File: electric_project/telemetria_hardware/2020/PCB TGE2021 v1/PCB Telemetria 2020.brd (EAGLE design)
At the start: 160 x 100 mm, 16 parts, among them IC1 INA240A1DR, IC2 MCP3221A6T-E_OTVAO, IC3 AZ1117IH-3.3TRG1

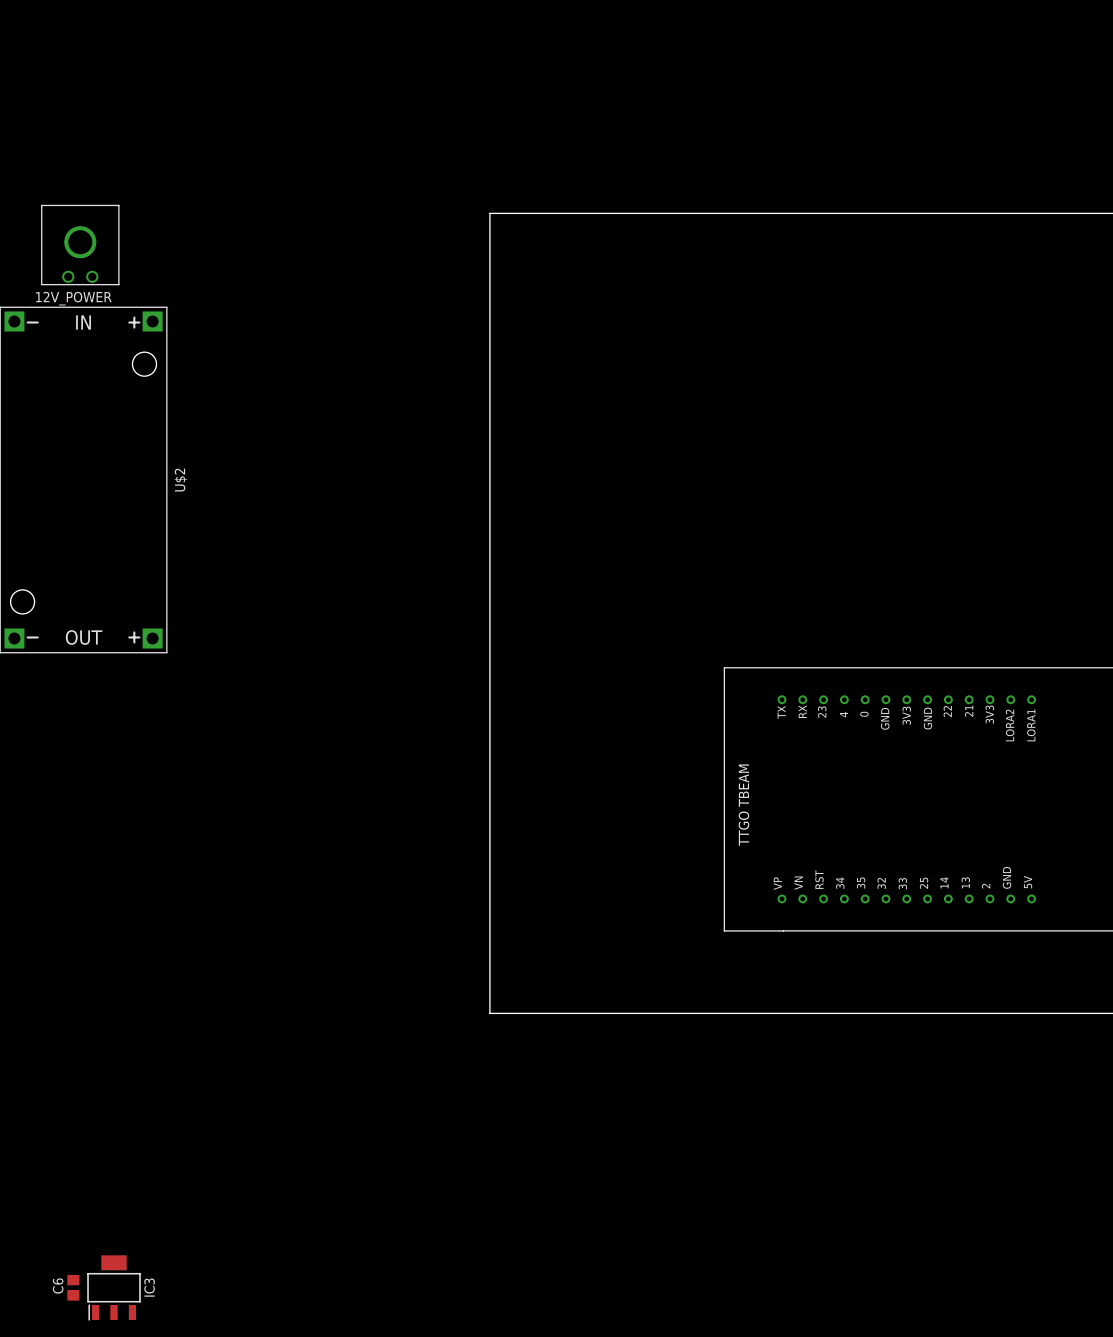
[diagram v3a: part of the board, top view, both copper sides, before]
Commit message: Ajustes de posicionamento no sch e brd
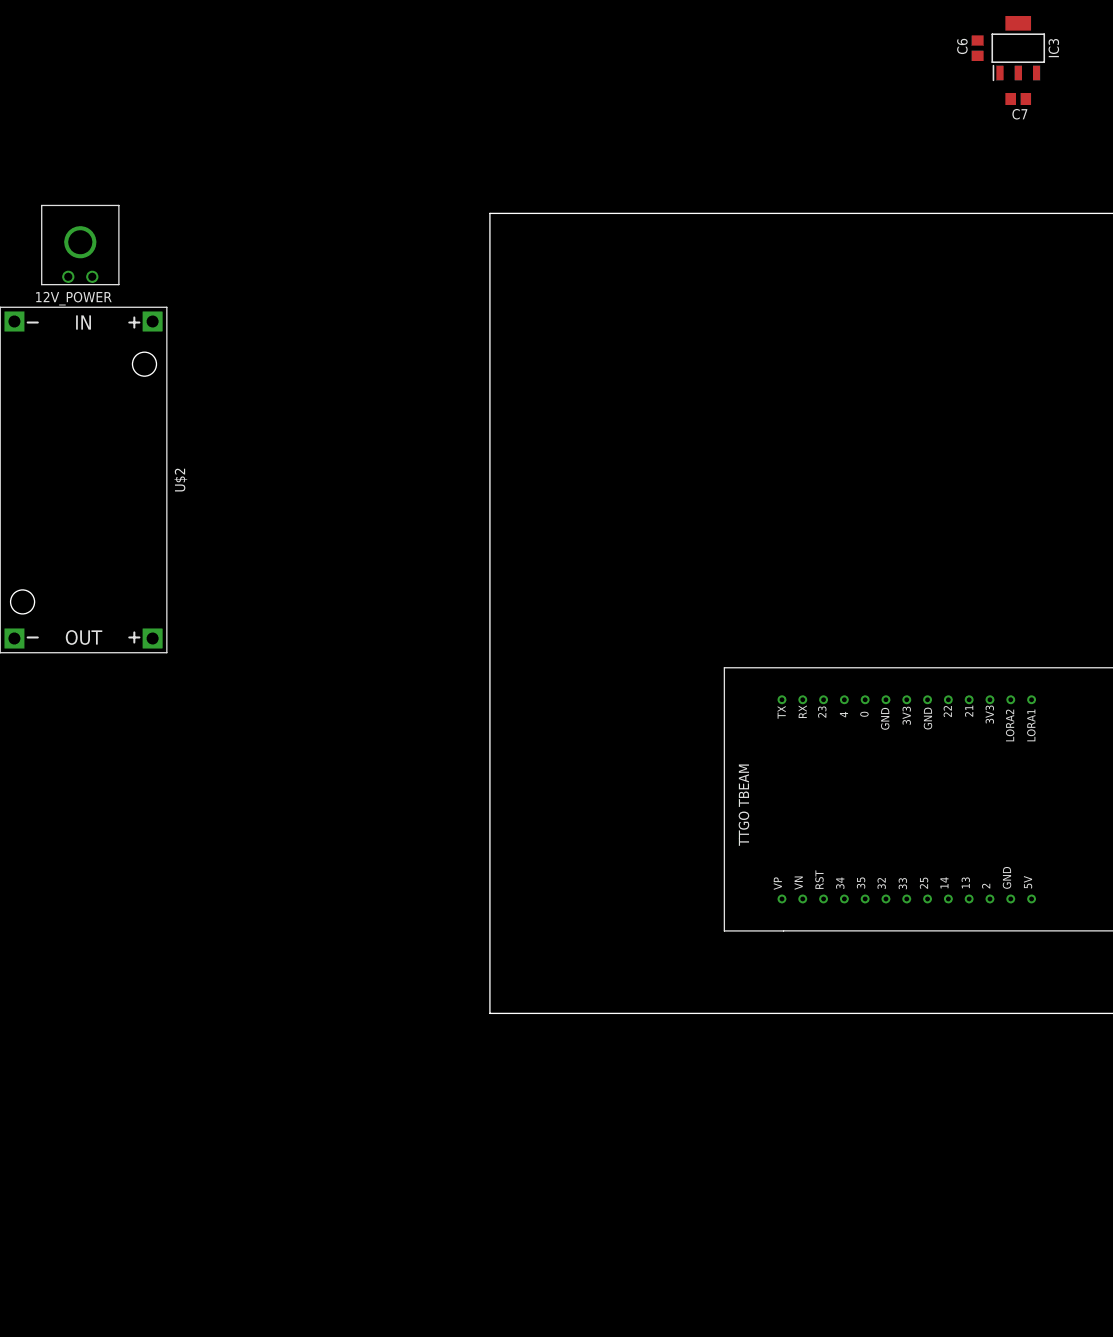
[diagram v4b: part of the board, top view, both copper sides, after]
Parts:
- added C7: 22uF, rcl:C0805
- moved C6 191.8 mm to (61.0, 120.7)
- moved IC3 191.8 mm to (66.0, 120.7)
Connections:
- net GND: now also C7.2
- net VCC_5V: now also C7.1
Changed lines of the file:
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@@
 <attribute name="VALUE" x="-52.705" y="92.075" size="1.27" layer="27" rot="R180" align="center"/>
 </element>
-<element name="IC3" library="AZ1117IH-3.3TRG1" package="SOT230P700X170-4N" value="AZ1117IH-3.3TRG1" x="-46.99" y="-34.29" smashed="yes" rot="R90">
-<attribute name="DESCRIPTION" value="LDO Voltage Regulators LDO BJT HiCurr 1.35A 10Hz to 10KHz" x="-46.99" y="-34.29" size="1.778" layer="27" rot="R90" display="off"/>
-<attribute name="HEIGHT" value="1.7mm" x="-46.99" y="-34.29" size="1.778" layer="27" rot="R90" display="off"/>
-<attribute name="MANUFACTURER_NAME" value="Diodes Inc." x="-46.99" y="-34.29" size="1.778" layer="27" rot="R90" display="off"/>
-<attribute name="MANUFACTURER_PART_NUMBER" value="AZ1117IH-3.3TRG1" x="-46.99" y="-34.29" size="1.778" layer="27" rot="R90" display="off"/>
-<attribute name="MOUSER_PART_NUMBER" value="621-AZ1117IH-3.3TRG1" x="-46.99" y="-34.29" size="1.778" layer="27" rot="R90" display="off"/>
-<attribute name="MOUSER_PRICE-STOCK" value="https://www.mouser.co.uk/ProductDetail/Diodes-Incorporated/AZ1117IH-33TRG1?qs=cpo3%2FpBou2jnS4SxLgAVoA%3D%3D" x="-46.99" y="-34.29" size="1.778" layer="27" rot="R90" display="off"/>
-<attribute name="NAME" x="-42.545" y="-34.29" size="1.27" layer="25" rot="R90" align="center"/>
-<attribute name="VALUE" x="-46.99" y="-34.29" size="1.27" layer="27" rot="R90" align="center"/>
+<element name="IC3" library="AZ1117IH-3.3TRG1" package="SOT230P700X170-4N" value="AZ1117IH-3.3TRG1" x="66.04" y="120.65" smashed="yes" rot="R90">
+<attribute name="DESCRIPTION" value="LDO Voltage Regulators LDO BJT HiCurr 1.35A 10Hz to 10KHz" x="66.04" y="120.65" size="1.778" layer="27" rot="R90" display="off"/>
+<attribute name="HEIGHT" value="1.7mm" x="66.04" y="120.65" size="1.778" layer="27" rot="R90" display="off"/>
+<attribute name="MANUFACTURER_NAME" value="Diodes Inc." x="66.04" y="120.65" size="1.778" layer="27" rot="R90" display="off"/>
+<attribute name="MANUFACTURER_PART_NUMBER" value="AZ1117IH-3.3TRG1" x="66.04" y="120.65" size="1.778" layer="27" rot="R90" display="off"/>
+<attribute name="MOUSER_PART_NUMBER" value="621-AZ1117IH-3.3TRG1" x="66.04" y="120.65" size="1.778" layer="27" rot="R90" display="off"/>
+<attribute name="MOUSER_PRICE-STOCK" value="https://www.mouser.co.uk/ProductDetail/Diodes-Incorporated/AZ1117IH-33TRG1?qs=cpo3%2FpBou2jnS4SxLgAVoA%3D%3D" x="66.04" y="120.65" size="1.778" layer="27" rot="R90" display="off"/>
+<attribute name="NAME" x="70.485" y="120.65" size="1.27" layer="25" rot="R90" align="center"/>
+<attribute name="VALUE" x="66.04" y="120.65" size="1.27" layer="27" rot="R90" align="center"/>
 </element>
-<element name="C6" library="rcl" library_urn="urn:adsk.eagle:library:334" package="C0805" package3d_urn="urn:adsk.eagle:package:23617/2" value="22uF" x="-52.07" y="-34.29" smashed="yes" rot="R270">
-<attribute name="NAME" x="-54.61" y="-33.02" size="1.27" layer="25" rot="R270"/>
-<attribute name="POPULARITY" value="63" x="-52.07" y="-34.29" size="1.778" layer="27" rot="R270" display="off"/>
-<attribute name="SPICEPREFIX" value="C" x="-52.07" y="-34.29" size="1.778" layer="27" rot="R270" display="off"/>
-<attribute name="VALUE" x="-54.61" y="-33.02" size="1.27" layer="27" rot="R270"/>
+<element name="C6" library="rcl" library_urn="urn:adsk.eagle:library:334" package="C0805" package3d_urn="urn:adsk.eagle:package:23617/2" value="22uF" x="60.96" y="120.65" smashed="yes" rot="R270">
+<attribute name="NAME" x="58.42" y="121.92" size="1.27" layer="25" rot="R270"/>
+<attribute name="POPULARITY" value="63" x="60.96" y="120.65" size="1.778" layer="27" rot="R270" display="off"/>
+<attribute name="SPICEPREFIX" value="C" x="60.96" y="120.65" size="1.778" layer="27" rot="R270" display="off"/>
+<attribute name="VALUE" x="58.42" y="121.92" size="1.27" layer="27" rot="R270"/>
+</element>
+<element name="C7" library="rcl" library_urn="urn:adsk.eagle:library:334" package="C0805" package3d_urn="urn:adsk.eagle:package:23617/2" value="22uF" x="66.04" y="114.3" smashed="yes" rot="R180">
+<attribute name="NAME" x="67.31" y="113.03" size="1.27" layer="25" rot="R180"/>
+<attribute name="POPULARITY" value="63" x="66.04" y="114.3" size="1.778" layer="27" rot="R180" display="off"/>
+<attribute name="SPICEPREFIX" value="C" x="66.04" y="114.3" size="1.778" layer="27" rot="R180" display="off"/>
+<attribute name="VALUE" x="67.31" y="116.84" size="1.27" layer="27" rot="R180"/>
 </element>
 </elements>
@@
 <contactref element="IC3" pad="1"/>
 <contactref element="C6" pad="2"/>
-<wire x1="65.105" y1="14.305" x2="49.505" y2="39.205" width="0" layer="19" extent="1-1"/>
-<wire x1="-59.436" y1="46.863" x2="49.505" y2="39.205" width="0" layer="19" extent="1-1"/>
+<contactref element="C7" pad="2"/>
+<wire x1="60.96" y1="119.7" x2="65.09" y2="114.3" width="0" layer="19" extent="1-1"/>
+<wire x1="63.74" y1="117.55" x2="60.96" y2="119.7" width="0" layer="19" extent="1-1"/>
+<wire x1="-59.436" y1="46.863" x2="60.96" y2="119.7" width="0" layer="19" extent="1-1"/>
 <wire x1="-59.436" y1="86.487" x2="-59.436" y2="46.863" width="0" layer="19" extent="1-1"/>
 <wire x1="-52.705" y1="92.075" x2="-59.436" y2="86.487" width="0" layer="19" extent="1-1"/>
-<wire x1="-49.29" y1="-37.39" x2="-59.436" y2="46.863" width="0" layer="19" extent="1-1"/>
-<wire x1="-52.07" y1="-35.24" x2="-49.29" y2="-37.39" width="0" layer="19" extent="1-1"/>
+<wire x1="49.505" y1="39.205" x2="-59.436" y2="46.863" width="0" layer="19" extent="1-1"/>
+<wire x1="65.105" y1="14.305" x2="49.505" y2="39.205" width="0" layer="19" extent="1-1"/>
 <wire x1="182.709" y1="97.155" x2="65.105" y2="14.305" width="0" layer="19" extent="1-1"/>
 <wire x1="188.131" y1="97.155" x2="182.709" y2="97.155" width="0" layer="19" extent="1-1"/>
@@
 <contactref element="IC3" pad="2"/>
 <wire x1="52.105" y1="39.205" x2="62.505" y2="39.205" width="0" layer="19" extent="1-1"/>
-<wire x1="-46.99" y1="-31.19" x2="52.105" y2="39.205" width="0" layer="19" extent="1-1"/>
-<wire x1="-46.99" y1="-37.39" x2="-46.99" y2="-31.19" width="0" layer="19" extent="1-1"/>
-<wire x1="-52.07" y1="-33.34" x2="-46.99" y2="-37.39" width="0" layer="19" extent="1-1"/>
+<wire x1="66.04" y1="123.75" x2="52.105" y2="39.205" width="0" layer="19" extent="1-1"/>
+<wire x1="66.04" y1="117.55" x2="66.04" y2="123.75" width="0" layer="19" extent="1-1"/>
+<wire x1="60.96" y1="121.6" x2="66.04" y2="117.55" width="0" layer="19" extent="1-1"/>
 <wire x1="180.34" y1="87.315" x2="62.505" y2="39.205" width="0" layer="19" extent="1-1"/>
 <wire x1="182.88" y1="87.315" x2="180.34" y2="87.315" width="0" layer="19" extent="1-1"/>
@@
 <contactref element="U$2" pad="OUT+"/>
 <contactref element="IC3" pad="3"/>
-<wire x1="-42.164" y1="46.863" x2="-44.69" y2="-37.39" width="0" layer="19" extent="1-1"/>
+<contactref element="C7" pad="1"/>
+<wire x1="68.34" y1="117.55" x2="66.99" y2="114.3" width="0" layer="19" extent="1-1"/>
+<wire x1="-42.164" y1="46.863" x2="68.34" y2="117.55" width="0" layer="19" extent="1-1"/>
 </signal>
 </signals>

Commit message: Renaming motor shunt signals
i had named the shunt signals with the sufix _N and _P but this is understood as differential signals on eagle.
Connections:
- net MSHUNT_N renamed MSHUNT_M
- net MSHUNT_P renamed MSHUNT_B
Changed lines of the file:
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@@
 </elements>
 <signals>
-<signal name="MSHUNT_N">
-<contactref element="IC1" pad="1"/>
-<contactref element="MSHUNT" pad="2"/>
-<wire x1="182.709" y1="98.425" x2="183.67" y2="104.735" width="0" layer="19" extent="1-1"/>
-</signal>
 <signal name="GND">
 <contactref element="IC1" pad="2"/>
@@
 <wire x1="189.865" y1="89.85" x2="192.405" y2="89.85" width="0" layer="19" extent="1-1"/>
 <wire x1="187.94" y1="89.535" x2="189.865" y2="89.85" width="0" layer="19" extent="1-1"/>
-</signal>
-<signal name="MSHUNT_P">
-<contactref element="IC1" pad="8"/>
-<contactref element="MSHUNT" pad="1"/>
-<wire x1="188.131" y1="98.425" x2="187.17" y2="104.735" width="0" layer="19" extent="1-1"/>
 </signal>
 <signal name="VCC_3V3">
@@
 <wire x1="-42.164" y1="46.863" x2="68.34" y2="117.55" width="0" layer="19" extent="1-1"/>
 </signal>
+<signal name="MSHUNT_M">
+<contactref element="IC1" pad="1"/>
+<contactref element="MSHUNT" pad="2"/>
+<wire x1="182.709" y1="98.425" x2="183.67" y2="104.735" width="0" layer="19" extent="1-1"/>
+</signal>
+<signal name="MSHUNT_B">
+<contactref element="IC1" pad="8"/>
+<contactref element="MSHUNT" pad="1"/>
+<wire x1="188.131" y1="98.425" x2="187.17" y2="104.735" width="0" layer="19" extent="1-1"/>
+</signal>
 </signals>

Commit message: Positioning parts on pcb for preview in fusion
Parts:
- added C8: (no value), rcl:C0805
- added IC4: ACS758LCB-050B-PFF-T, allegro:CB-PFF
- moved 12V_POWER 217.1 mm to (149.9, 14.0), turned to 90 degrees
- moved U$2 184.0 mm to (125.1, 12.7), turned to 180 degrees
- moved C6 121.4 mm to (91.4, 3.17), turned to 0 degrees
- moved IC3 115.2 mm to (91.4, 8.26), turned to 180 degrees
- moved C7 110.7 mm to (97.8, 8.26), turned to 270 degrees
- moved C2 42.3 mm to (155.6, 78.7)
- moved C4 42.3 mm to (151.8, 70.5)
- moved C1 42.3 mm to (153.0, 78.7)
- moved C3 42.3 mm to (154.3, 70.5)
- moved C5 42.3 mm to (152.7, 74.3)
- moved IC1 42.3 mm to (147.3, 78.1)
- moved IC2 42.3 mm to (148.6, 71.1)
- moved MSHUNT 42.3 mm to (147.3, 90.2)
- moved R1 42.3 mm to (142.2, 69.8)
- moved R2 42.3 mm to (144.8, 69.8)
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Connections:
- new net MPPT_COUT: IC4.3
- net GND: now also C8.2, IC4.2
- net VCC_3V3: now also C8.1, IC4.1

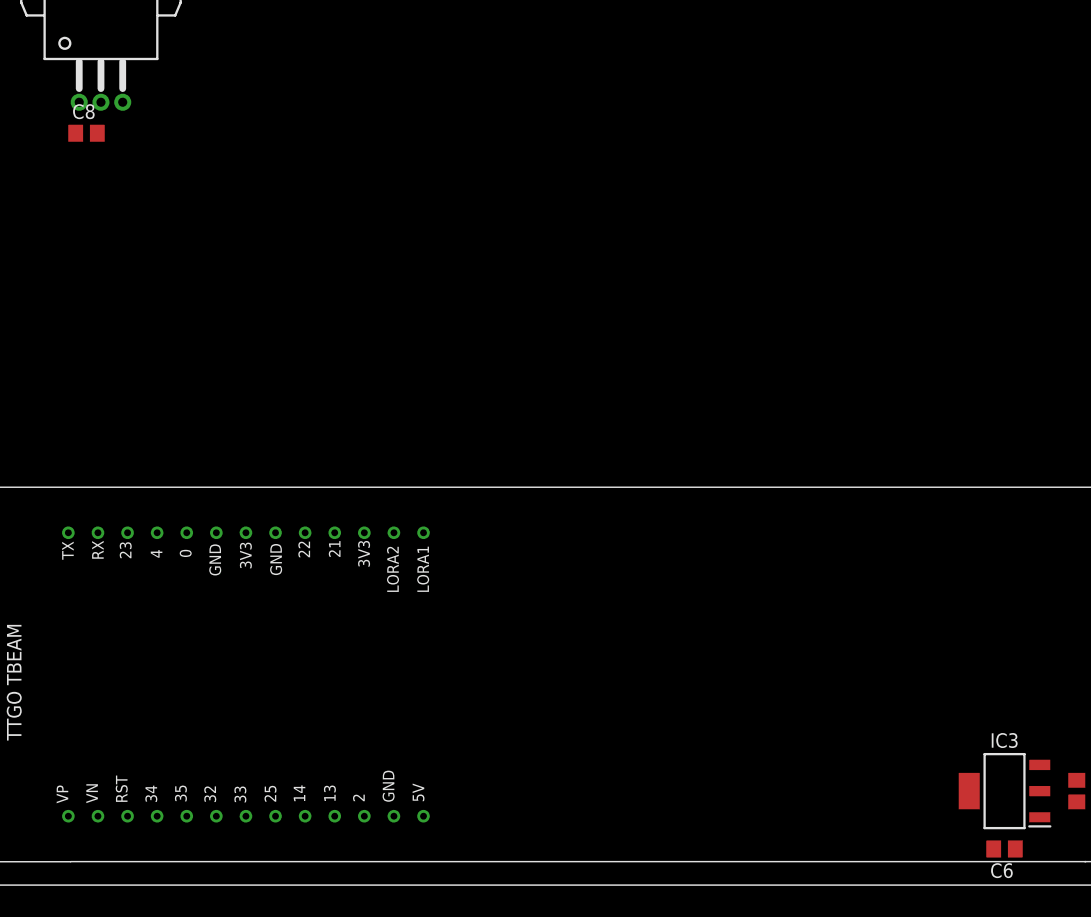
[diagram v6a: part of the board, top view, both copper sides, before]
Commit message: Just updating past commit (MPPT current measurement)
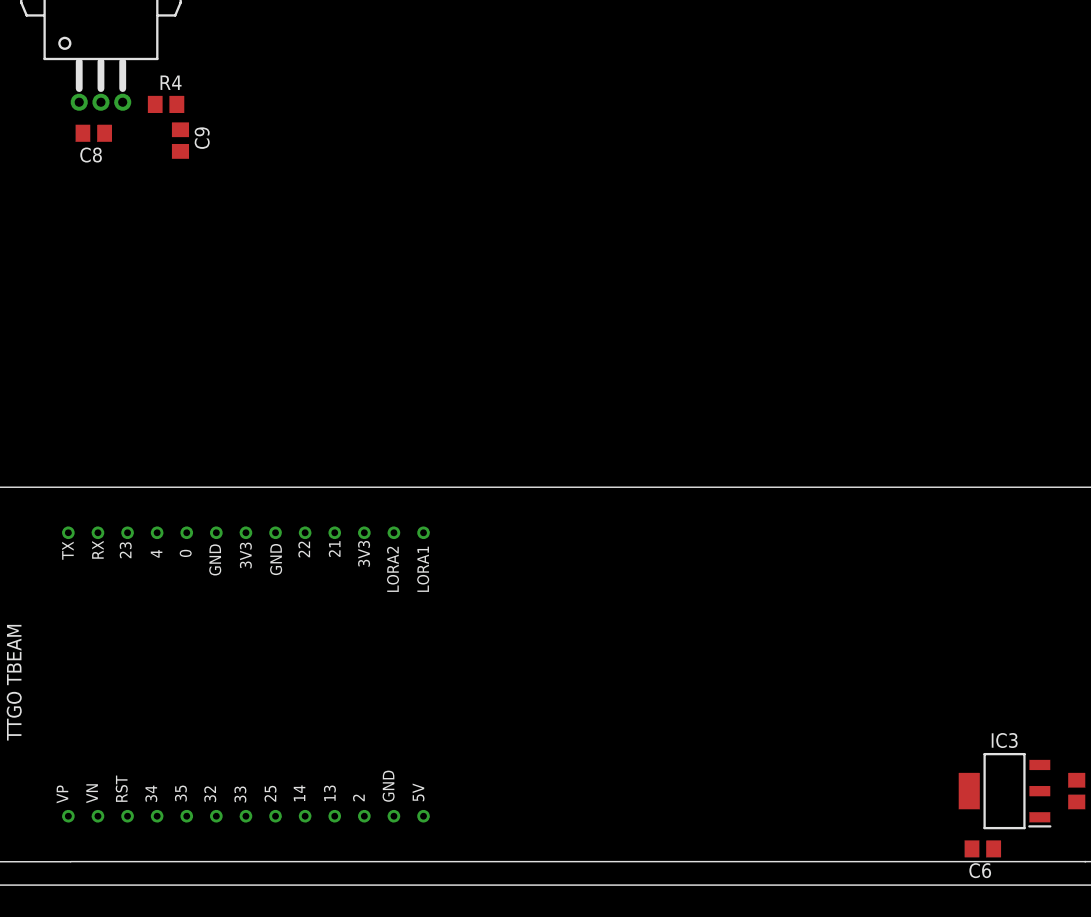
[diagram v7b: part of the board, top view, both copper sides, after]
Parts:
- added C9: 100nF, rcl:C0805
- added R4: 4.7k, rcl:R0805
- C8: value (none) -> 100nF
- moved C6 1.91 mm to (89.5, 3.17)
- moved C8 0.63 mm to (11.4, 66.0)
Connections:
- removed net MPPT_COUT: IC4.3
- new net CMPPT_F: C9.1, R4.2
- new net CMPPT_M: IC4.IP-, IC4.IP-@10, IC4.IP-@11, IC4.IP-@12, IC4.IP-@13, IC4.IP-@14, IC4.IP-@15, IC4.IP-@16, IC4.IP-@17, IC4.IP-@2, IC4.IP-@3, IC4.IP-@4, IC4.IP-@5, IC4.IP-@6, IC4.IP-@7, IC4.IP-@8, IC4.IP-@9
- new net CMPPT_OUT: IC4.3, R4.1
- new net CMPPT_P: IC4.IP+, IC4.IP+@10, IC4.IP+@11, IC4.IP+@12, IC4.IP+@13, IC4.IP+@14, IC4.IP+@15, IC4.IP+@16, IC4.IP+@17, IC4.IP+@2, IC4.IP+@3, IC4.IP+@4, IC4.IP+@5, IC4.IP+@6, IC4.IP+@7, IC4.IP+@8, IC4.IP+@9
- net GND: now also C9.2
